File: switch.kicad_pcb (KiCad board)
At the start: 2 copper layers, 48.3 x 67.9 mm, 33 parts, among them IC1 ATTINY24, IC2 MCP2515, IC3 MCP2551, J1 RJ11, J2 RJ11, K1 RELAY_G6D, K2 RELAY_G6D, K3 RELAY_G6D, K4 RELAY_G6D, P1 CONN_PROG_AVR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

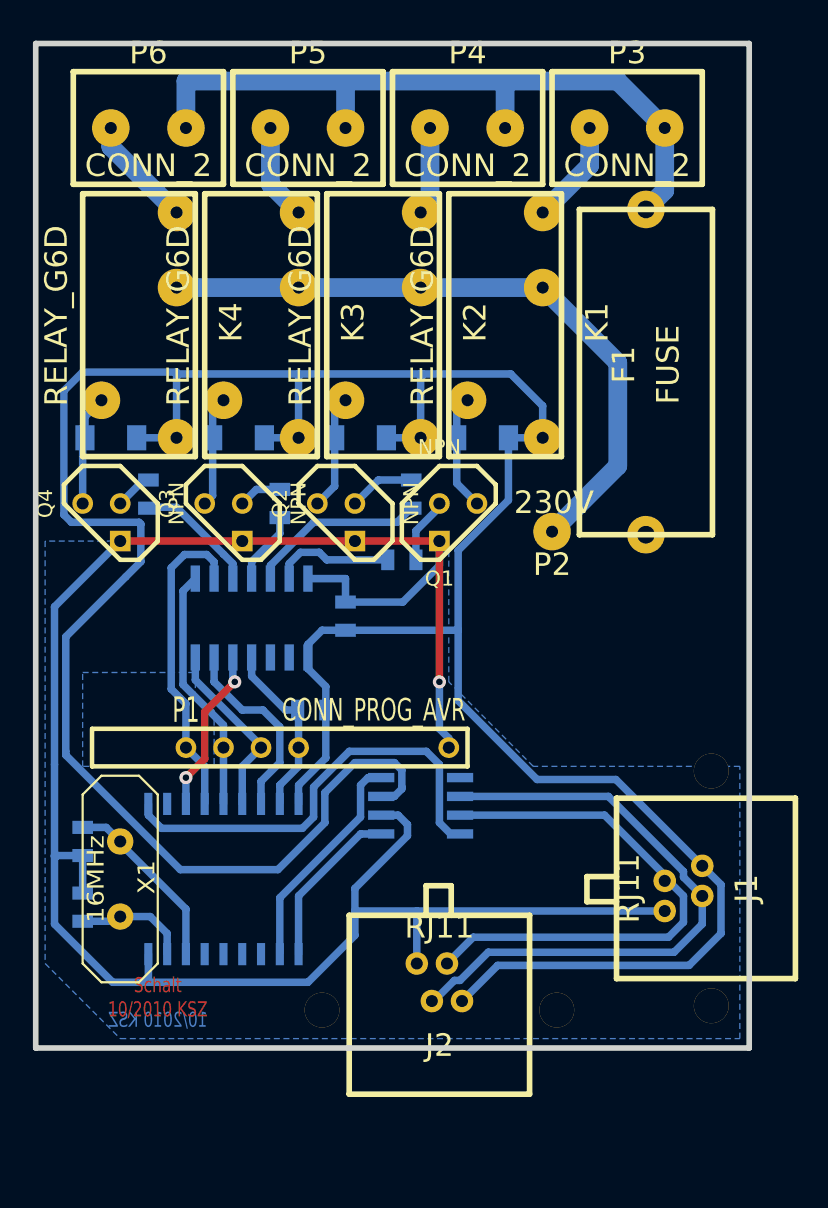
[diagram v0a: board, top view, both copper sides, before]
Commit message: Update switching module
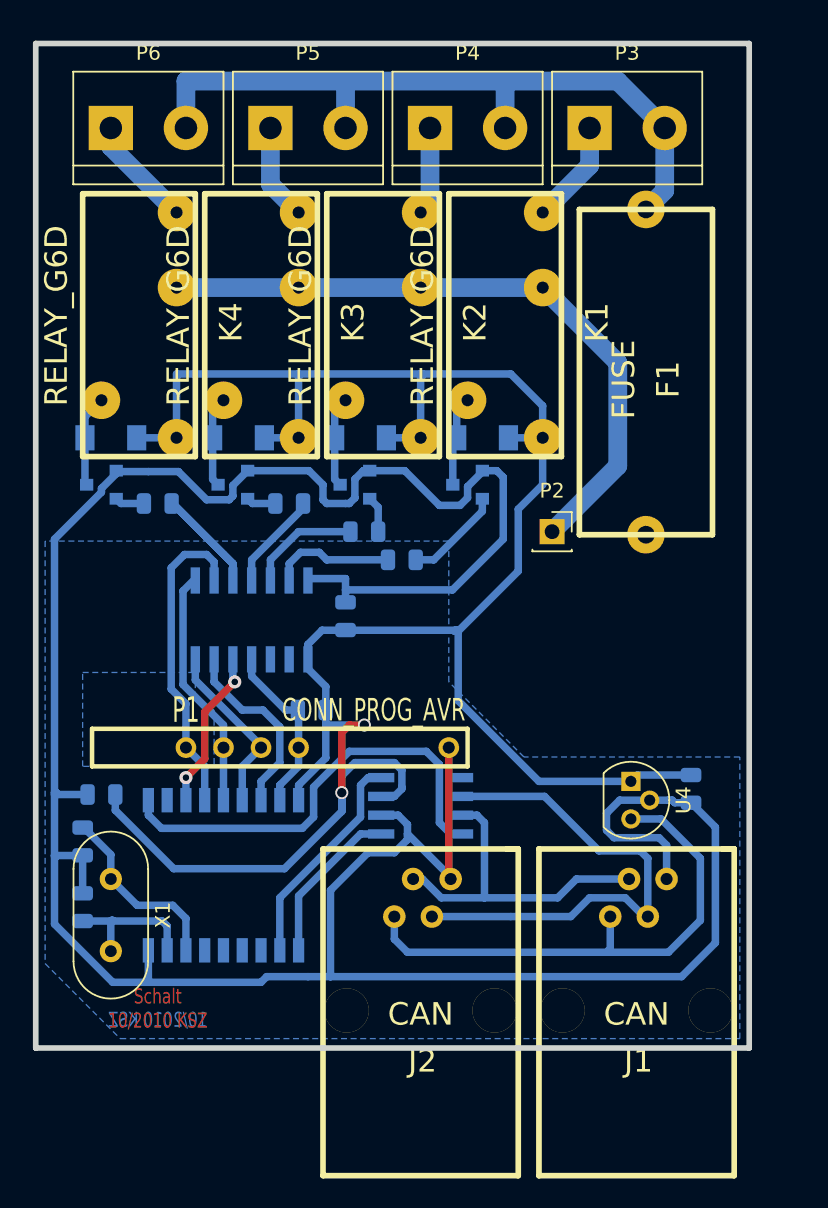
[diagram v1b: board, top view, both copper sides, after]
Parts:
- removed IC1: ATTINY24, SOIC14_150
- removed IC2: MCP2515, SOIC18_300
- removed IC3: MCP2551, SOIC8_150
- added C4: 100n, Capacitor_SMD:C_0805_2012Metric, B.Cu at (17.8, 64.1)
- added C5: 2.2u, Capacitor_SMD:C_0805_2012Metric, B.Cu at (57.7, 63.8)
- added U1: ATTINY24, ICs_SMD_K:SOIC14_150, B.Cu at (27.9, 52.2)
- added U2: MCP2515, ICs_SMD_K:SOIC18_300, B.Cu at (26.0, 69.6)
- added U3: MCP2551, ICs_SMD_K:SOIC8_150, B.Cu at (39.4, 64.9)
- added U4: LP2950-5.0_TO92, Package_TO_SOT_THT:TO-92, F.Cu at (53.6, 63.2)
- C1, C2, C3: footprint SM0805 -> Capacitor_SMD:C_0805_2012Metric
- D1, D2, D3, D4: footprint Diode-MiniMELF_Standard_RevA_27July2010 -> Diode_SMD:D_MiniMELF
- F1: footprint FUSE_PRINT -> Connectors_K:FUSE_PRINT
- J1, J2: value RJ11 -> CAN; footprint RJ11_RN -> Connectors_K:RJ11_RO
- K1, K2, K3, K4: footprint RELAY_G6D -> Discrete_K:RELAY_G6D
- P1: footprint SIL-10_MYAVR -> Connectors_K:SIL-10_MYAVR
- P2: footprint PAD -> Connector_PinSocket_2.54mm:PinSocket_1x01_P2.54mm_Vertical
- P3, P4, P5, P6: value CONN_2 -> Pump; footprint CONN_AKL2 -> TerminalBlock:TerminalBlock_bornier-2_P5.08mm
- Q1: footprint TO92-INVERT -> Package_TO_SOT_SMD:SOT-23; moved to B.Cu
- Q2, Q3, Q4: footprint TO92 -> Package_TO_SOT_SMD:SOT-23; moved to B.Cu
- R1, R2, R3, R4, R5: footprint SM0805 -> Resistor_SMD:R_0805_2012Metric
- X1: footprint HC-18UV -> Crystal:Crystal_HC49-U_Vertical
- moved J1 9.38 mm to (54.0, 78.7), turned to 0 degrees
- moved R3 4.07 mm to (35.6, 46.4), turned to 180 degrees
- moved Q2 2.84 mm to (34.9, 43.2), turned to 180 degrees
- moved Q1 2.62 mm to (42.5, 43.2), turned to 180 degrees
- moved Q3 2.62 mm to (26.7, 43.2), turned to 180 degrees
- moved P3 2.54 mm to (50.8, 19.1)
- moved P4 2.54 mm to (40.0, 19.1)
- moved P5 2.54 mm to (29.2, 19.1)
- moved P6 2.54 mm to (18.4, 19.1)
- moved Q4 2.54 mm to (17.8, 43.2), turned to 180 degrees
- moved J2 1.42 mm to (39.4, 78.7)
- moved R5 0.90 mm to (21.6, 44.5), turned to 0 degrees
- moved R4 0.64 mm to (30.5, 44.5), turned to 0 degrees
- moved X1 0.64 mm to (18.4, 69.8)
- turned D1 to 180 degrees
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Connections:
- D1 pad 1: N-000029 -> +5V
- D1 pad 2: +5V -> Net-(D1-Pad2)
- D2 pad 1: N-000030 -> +5V
- D2 pad 2: +5V -> Net-(D2-Pad2)
- D3 pad 1: N-000031 -> +5V
- D3 pad 2: +5V -> Net-(D3-Pad2)
- D4 pad 1: N-000032 -> +5V
- D4 pad 2: +5V -> Net-(D4-Pad2)
- F1 pad 1: (no net) -> /230V+
- F1 pad 2: /230V+ -> Net-(F1-Pad2)
- J1 pad 2: +5V -> Net-(J1-Pad2)
- J2 pad 2: +5V -> Net-(J1-Pad2)
- K1 pad 13: N-000029 -> Net-(D1-Pad2)
- K2 pad 13: N-000030 -> Net-(D2-Pad2)
- K3 pad 13: N-000031 -> Net-(D3-Pad2)
- K4 pad 13: N-000032 -> Net-(D4-Pad2)
- Q1 pad 3: N-000029 -> Net-(D1-Pad2)
- Q2 pad 3: N-000030 -> Net-(D2-Pad2)
- Q3 pad 3: N-000031 -> Net-(D3-Pad2)
- Q4 pad 3: N-000032 -> Net-(D4-Pad2)
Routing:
- net +5V: track 211.5 -> 151.9 mm, vias 0 -> 2
- net GND: track 142.1 -> 196.3 mm, vias 1 -> 0
- net Net-(J1-Pad2): track 0.00 -> 36.2 mm
- net Net-(U2-Pad10): track 0.00 -> 30.2 mm
- net N-000005: track 30.2 -> 0.00 mm
- net Net-(U2-Pad2): track 0.00 -> 15.3 mm
- net N-000007: track 15.3 -> 0.00 mm
- net Net-(J1-Pad3): track 36.5 -> 22.6 mm
- net Net-(U1-Pad6): track 0.00 -> 13.1 mm
- net N-000011: track 13.1 -> 0.00 mm
- net Net-(U1-Pad5): track 0.00 -> 11.3 mm, vias 0 -> 2
- net N-000013: track 11.3 -> 0.00 mm, vias 2 -> 0
- net Net-(U2-Pad1): track 0.00 -> 11.3 mm
- net N-000008: track 11.3 -> 0.00 mm
- net N-000029: track 7.86 -> 0.00 mm
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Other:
- net class 230V: clearance 1.16078 -> 1.016
